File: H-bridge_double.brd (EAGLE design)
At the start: 47.9 x 36.8 mm, 34 parts, among them Q1 2N2222A, Q2 2N2222A, Q3 2N2907, Q4 2N2907, Q5 2N2222A, Q6 2N2222A, Q7 2N2907, Q8 2N2907, X1 22-23-2051, X3 22-23-2051

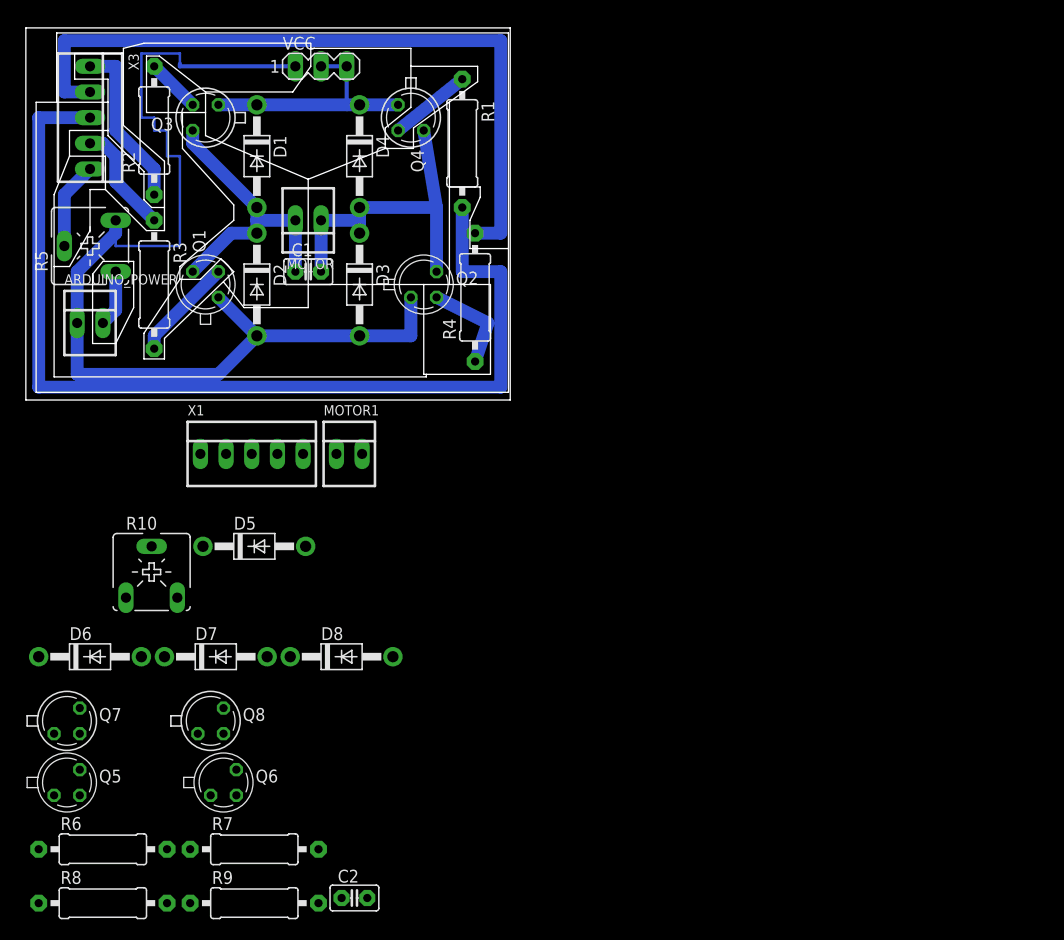
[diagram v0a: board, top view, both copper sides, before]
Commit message: Eagle CAD for Dual H-bridge
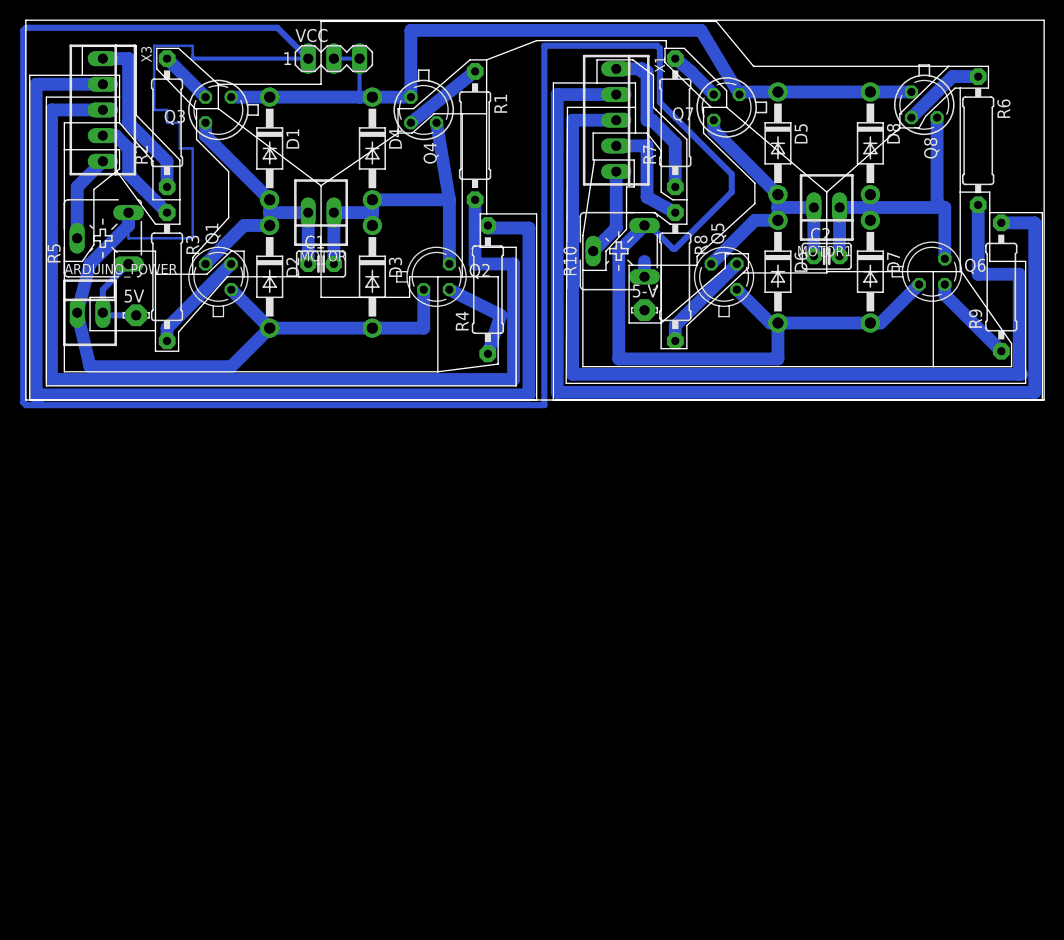
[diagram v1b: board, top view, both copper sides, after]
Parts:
- added 5-V, 5V: LSP10, solpad:LSP10
- moved R6 111.4 mm to (94.2, 25.7), turned to 270 degrees
- moved R9 95.8 mm to (96.5, 11.2), turned to 90 degrees
- moved Q8 93.3 mm to (88.9, 29.2), turned to 270 degrees
- moved Q7 89.1 mm to (69.3, 29.0), turned to 180 degrees
- moved Q6 86.4 mm to (89.7, 12.7)
- moved R8 84.0 mm to (64.3, 12.2), turned to 270 degrees
- moved R7 83.1 mm to (64.3, 27.4), turned to 90 degrees
- moved Q5 82.0 mm to (69.1, 12.2), turned to 90 degrees
- moved C2 78.8 mm to (79.2, 14.2)
- moved D6 78.0 mm to (74.4, 12.7), turned to 270 degrees
- moved D7 75.1 mm to (83.6, 12.7), turned to 270 degrees
- moved D8 72.9 mm to (83.6, 25.4), turned to 270 degrees
- moved D5 65.4 mm to (74.4, 25.4), turned to 270 degrees
- moved R10 56.1 mm to (58.7, 14.7), turned to 90 degrees
- moved MOTOR1 53.2 mm to (79.2, 19.1), turned to 180 degrees
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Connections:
- new net N$19: 5V.MP, ARDUINO_POWER.2, R5.A
- net N$15: now also 5-V.MP; no longer ARDUINO_POWER.2, R5.A
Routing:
- net GND: track 108.9 -> 358.0 mm
- net N$17: track 0.00 -> 102.6 mm
- net N$24: track 0.00 -> 94.7 mm
- net N$9: track 24.1 -> 84.1 mm
- net N$7: track 72.4 -> 107.2 mm
- net N$16: track 0.00 -> 32.0 mm
- net N$18: track 0.00 -> 29.3 mm
- net N$22: track 0.00 -> 16.2 mm
- net N$23: track 0.00 -> 11.3 mm
- net N$21: track 0.00 -> 10.1 mm
- net N$19: track 0.00 -> 9.29 mm
- net N$6: track 0.00 -> 8.92 mm
- net N$25: track 0.00 -> 8.82 mm
- net N$4: track 0.00 -> 8.29 mm
- net N$20: track 0.00 -> 5.22 mm
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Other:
- board size 47.9 x 36.8 mm -> 100.8 x 37.6 mm
